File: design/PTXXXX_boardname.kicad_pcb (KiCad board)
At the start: 4 copper layers, 150 x 100 mm, 5 parts

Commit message: changed to 0.20/0.20mm track/gap design rules match F.Fab text ...though F.Fab text previously had gap less than design rules ...picked new sensible based on Qucs studio calc 89.3ohm Zdiff
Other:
- board text added: "INSTRUCTIONS: =========== MULTILAYER, SURFACE MOUNT & THROUGH HOLE 4 (2 SIGNAL & POUR, 2 SPLIT PLANE) MIN 0.20MM TRACK / 0.20MM GAP / 0.30MM DRILL 90Z DIFF PAIR, OUTER 0.20MM TRACK / 0.20MM GAP 0.40MM PLANE CLEARANCE, 0.12MM TO INNER FR4 OR EQUIVALENT, PCB RATED UL94V-0 35um OUTERS AND 17.5um INNERS ENIG GREEN WHITE 100.0MM X 150.0MM 1.6MM +/- 10% MAX OVER PLATING NOT REQUIRED NOT REQUIRED NOT RE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"
- board text removed: "INSTRUCTIONS: =========== MULTILAYER, SURFACE MOUNT & THROUGH HOLE 4 (2 SIGNAL & POUR, 2 SPLIT PLANE) MIN 0.2MM TRACK / 0.20MM GAP / 0.30MM DRILL 90Z DIFF PAIR, OUTER (0.25MM TRACK / 0.15MM GAP / 0.12MM TO INNER) FR4 OR EQUIVALENT, PCB RATED UL94V-0 35um OUTERS AND 17.5um INNERS ENIG GREEN WHITE 100.0MM X 150.0MM 1.6MM +/- 10% MAX OVER PLATING NOT REQUIRED NOT REQUIRED NOT REQUIRED SEEK APPROVAL 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"
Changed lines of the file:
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@@
       (layer "B.SilkS" (type "Bottom Silk Screen") (color "White"))
       (copper_finish "ENIG")
-      (dielectric_constraints no)
+      (dielectric_constraints yes)
     )
     (pad_to_mask_clearance 0.065)
@@
     (effects (font (size 2.5 2.5) (thickness 0.25) italic) (justify left))
   )
-  (gr_text "FABRICATION\n===========\nSUMMARY:\nLAYER COUNT:\nDESIGN RULES:\nIMPEDANCE CONTROL:\n\nMATERIAL:\nCOPPER WEIGHT:\nFINISH:\nRESIST COLOUR:\nSILKSCREEN COLOUR:\nDIMENSIONS:\nFINISHED THICKNESS:\nEDGE PLATING:\nEDGE CONNECTORS:\nEDGE CHAMFERING:\nTHIEVING/VENTING:\nROHS/LEAD FREE:\nDRILLING:\nPLUGGING:\nOTHER NOTES:" (at 225.2 114.9) (layer "F.Fab")
+  (gr_text "FABRICATION\n===========\nSUMMARY:\nLAYER COUNT:\nDESIGN RULES:\nIMPEDANCE CONTROL:\n\n\nMATERIAL:\nCOPPER WEIGHT:\nFINISH:\nRESIST COLOUR:\nSILKSCREEN COLOUR:\nDIMENSIONS:\nFINISHED THICKNESS:\nEDGE PLATING:\nEDGE CONNECTORS:\nEDGE CHAMFERING:\nTHIEVING/VENTING:\nROHS/LEAD FREE:\nDRILLING:\nPLUGGING:\nOTHER NOTES:" (at 225.2 114.9) (layer "F.Fab")
     (effects (font (size 1.2 1.2) (thickness 0.2)) (justify right))
   )
-  (gr_text "INSTRUCTIONS:\n===========\nMULTILAYER, SURFACE MOUNT & THROUGH HOLE\n4 (2 SIGNAL & POUR, 2 SPLIT PLANE)\nMIN 0.2MM TRACK / 0.20MM GAP / 0.30MM DRILL\n90Z DIFF PAIR, OUTER\n    (0.25MM TRACK / 0.15MM GAP / 0.12MM TO INNER)\nFR4 OR EQUIVALENT, PCB RATED UL94V-0\n35um OUTERS AND 17.5um INNERS\nENIG\nGREEN\nWHITE\n100.0MM X 150.0MM\n1.6MM +/- 10% MAX OVER PLATING\nNOT REQUIRED\nNOT REQUIRED\nNOT REQUIRED\nSEEK APPROVAL\nYES\nSEE DRILL FILE. HOLE SIZES ARE FINISHED.\nNOT REQUIRED\nNONE" (at 226.2 114.9) (layer "F.Fab")
+  (gr_text "INSTRUCTIONS:\n===========\nMULTILAYER, SURFACE MOUNT & THROUGH HOLE\n4 (2 SIGNAL & POUR, 2 SPLIT PLANE)\nMIN 0.20MM TRACK / 0.20MM GAP / 0.30MM DRILL\n90Z DIFF PAIR, OUTER\n    0.20MM TRACK / 0.20MM GAP\n    0.40MM PLANE CLEARANCE, 0.12MM TO INNER\nFR4 OR EQUIVALENT, PCB RATED UL94V-0\n35um OUTERS AND 17.5um INNERS\nENIG\nGREEN\nWHITE\n100.0MM X 150.0MM\n1.6MM +/- 10% MAX OVER PLATING\nNOT REQUIRED\nNOT REQUIRED\nNOT REQUIRED\nSEEK APPROVAL\nYES\nSEE DRILL FILE. HOLE SIZES ARE FINISHED.\nNOT REQUIRED\nNONE" (at 226.2 114.9) (layer "F.Fab")
     (effects (font (size 1.2 1.2) (thickness 0.2)) (justify left))
   )

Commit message: fixes for edge clearance issue in v6... ...moved 'Margin' line to Eco2 layer ...(Margin interferes with copper in v6) ...changed Margin layer text from "Board Edge Placement Margin" ...now text "Board Edge Copper Margin" changed schematic DRCs rules to reduce number... ...changed library symbol from warning to ignore (too many) updated library ref for latest
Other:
- board text added: "Layer Name: Margin Layer Description: Board Edge Copper Margin"
- board text removed: "Layer Name: Margin Layer Description: Board Edge Placement Margin"
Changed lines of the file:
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@@
       (xy 58.6 154.1)
     ) (layer "F.SilkS") (width 0.1) (fill solid))
+  (gr_line (start 188.5 158.5) (end 41.5 158.5) (layer "Eco2.User") (width 0.15))
+  (gr_line (start 41.5 61.5) (end 188.5 61.5) (layer "Eco2.User") (width 0.15))
+  (gr_line (start 188.5 61.5) (end 188.5 158.5) (layer "Eco2.User") (width 0.15))
+  (gr_line (start 41.5 158.5) (end 41.5 61.5) (layer "Eco2.User") (width 0.15))
   (gr_line (start 40 60) (end 40 160) (layer "Edge.Cuts") (width 0.05))
   (gr_line (start 190 160) (end 190 60) (layer "Edge.Cuts") (width 0.05))
   (gr_line (start 190 60) (end 40 60) (layer "Edge.Cuts") (width 0.05))
   (gr_line (start 40 160) (end 190 160) (layer "Edge.Cuts") (width 0.05))
-  (gr_line (start 188.5 158.5) (end 41.5 158.5) (layer "Margin") (width 0.15))
-  (gr_line (start 41.5 61.5) (end 188.5 61.5) (layer "Margin") (width 0.15))
-  (gr_line (start 188.5 61.5) (end 188.5 158.5) (layer "Margin") (width 0.15))
-  (gr_line (start 41.5 158.5) (end 41.5 61.5) (layer "Margin") (width 0.15))
   (gr_poly
     (pts
@@
     (effects (font (size 2.5 2.5) (thickness 0.25) italic) (justify left))
   )
-  (gr_text "Layer Name:          Margin\nLayer Description:    Board Edge Placement Margin" (at 67.2 27.4) (layer "Margin")
+  (gr_text "Layer Name:          Margin\nLayer Description:    Board Edge Copper Margin" (at 67.2 27.4) (layer "Margin")
     (effects (font (size 2.5 2.5) (thickness 0.25) italic) (justify left))
   )

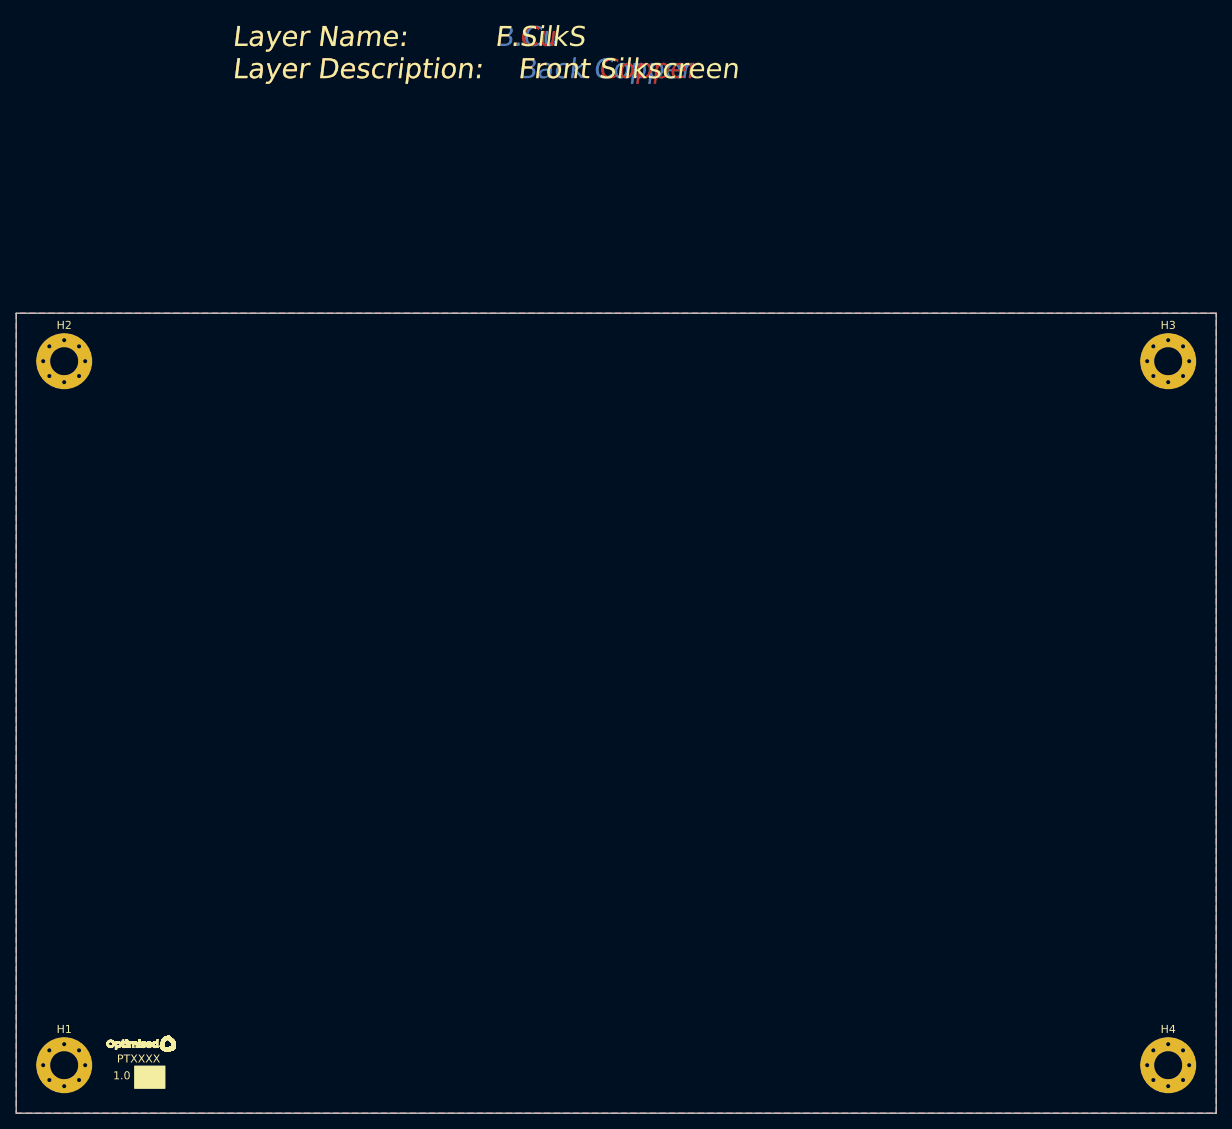
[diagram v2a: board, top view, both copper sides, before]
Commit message: added Fiducials FID1-6 using new library part... ...3off top, 3off bottom, 1mm/3mm mask default but 2mm available ...annotated, netlisted, placed in PCB updated library ref for latest
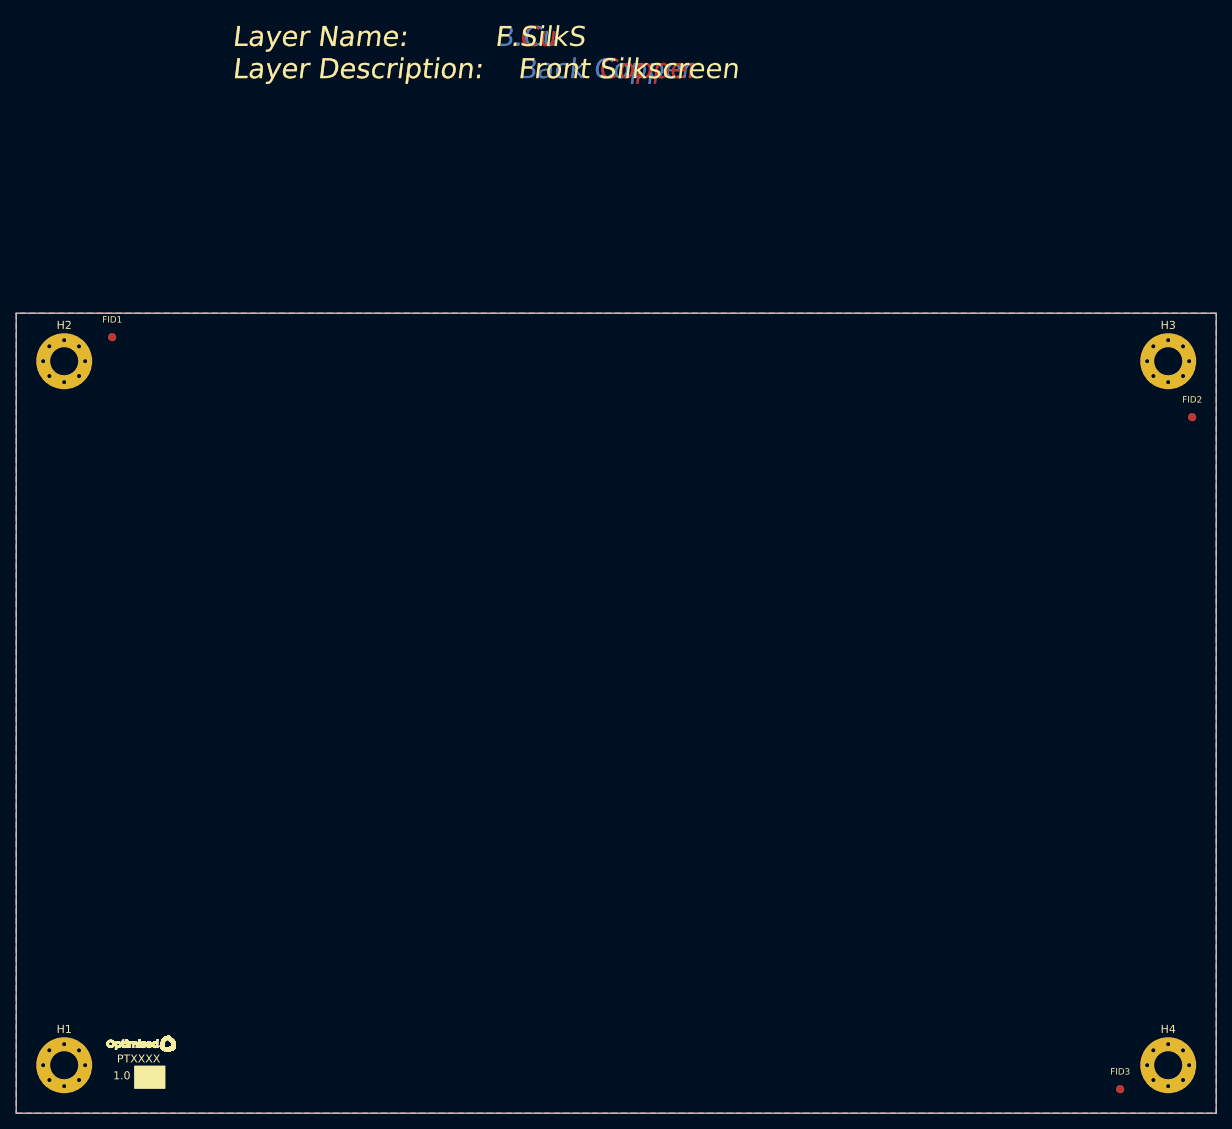
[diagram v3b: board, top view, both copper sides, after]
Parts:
- added FID1: Fiducial, _kb_miscellaneous:Fiducial_1mm_Mask3mm, F.Cu at (52.0, 63.0)
- added FID2: Fiducial, _kb_miscellaneous:Fiducial_1mm_Mask3mm, F.Cu at (187.0, 73.0)
- added FID3: Fiducial, _kb_miscellaneous:Fiducial_1mm_Mask3mm, F.Cu at (178.0, 157.0)
- added FID4: Fiducial, _kb_miscellaneous:Fiducial_1mm_Mask3mm, B.Cu at (178.0, 157.0)
- added FID5: Fiducial, _kb_miscellaneous:Fiducial_1mm_Mask3mm, B.Cu at (187.0, 73.0)
- added FID6: Fiducial, _kb_miscellaneous:Fiducial_1mm_Mask3mm, B.Cu at (52.0, 63.0)
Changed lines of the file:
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@@
       ) (layer "F.SilkS") (width 0.01) (fill solid))
+  )
+  (footprint "_kb_miscellaneous:Fiducial_1mm_Mask3mm" (layer "F.Cu")
+    (at 187 73)
+    (descr "Circular Fiducial, 1mm bare copper, 3mm soldermask opening (recommended)")
+    (tags "fiducial")
+    (property "Description" "Fiducial Assembly Marker")
+    (property "FitPart" "DNF")
+    (property "MPN1" "N/A")
+    (property "MPN2" " ")
+    (property "Manufacturer1" "N/A")
+    (property "Manufacturer2" " ")
+    (property "SKU1" " ")
+    (property "SKU2" " ")
+    (property "Sheetfile" "PTXXXX_boardname.kicad_sch")
+    (property "Sheetname" "")
+    (property "Vendor1" " ")
+    (property "Vendor2" " ")
+    (attr smd)
+    (fp_text reference "FID2" (at 0 -2.2) (layer "F.SilkS")
+      (effects (font (size 0.8 0.8) (thickness 0.12)))
+    )
+    (fp_text value "Fiducial" (at 0 2.286) (layer "F.Fab") hide
+      (effects (font (size 1 1) (thickness 0.15)))
+    )
+    (fp_text user "${REFERENCE}" (at 0 0) (layer "F.Fab")
+      (effects (font (size 0.6 0.6) (thickness 0.1)))
+    )
+    (fp_circle (center 0 0) (end 1.6 0) (layer "F.CrtYd") (width 0.05) (fill none))
+    (fp_circle (center 0 0) (end 1.5 0) (layer "F.Fab") (width 0.1) (fill none))
+    (pad "" smd circle (at 0 0) (size 1 1) (property pad_prop_fiducial_glob) (layers "F.Cu" "F.Mask")
+      (solder_mask_margin 1) (clearance 1))
+  )
+  (footprint "_kb_miscellaneous:Fiducial_1mm_Mask3mm" (layer "F.Cu")
+    (at 178 157)
+    (descr "Circular Fiducial, 1mm bare copper, 3mm soldermask opening (recommended)")
+    (tags "fiducial")
+    (property "Description" "Fiducial Assembly Marker")
+    (property "FitPart" "DNF")
+    (property "MPN1" "N/A")
+    (property "MPN2" " ")
+    (property "Manufacturer1" "N/A")
+    (property "Manufacturer2" " ")
+    (property "SKU1" " ")
+    (property "SKU2" " ")
+    (property "Sheetfile" "PTXXXX_boardname.kicad_sch")
+    (property "Sheetname" "")
+    (property "Vendor1" " ")
+    (property "Vendor2" " ")
+    (attr smd)
+    (fp_text reference "FID3" (at 0 -2.2) (layer "F.SilkS")
+      (effects (font (size 0.8 0.8) (thickness 0.12)))
+    )
+    (fp_text value "Fiducial" (at 0 2.286) (layer "F.Fab") hide
+      (effects (font (size 1 1) (thickness 0.15)))
+    )
+    (fp_text user "${REFERENCE}" (at 0 0) (layer "F.Fab")
+      (effects (font (size 0.6 0.6) (thickness 0.1)))
+    )
+    (fp_circle (center 0 0) (end 1.6 0) (layer "F.CrtYd") (width 0.05) (fill none))
+    (fp_circle (center 0 0) (end 1.5 0) (layer "F.Fab") (width 0.1) (fill none))
+    (pad "" smd circle (at 0 0) (size 1 1) (property pad_prop_fiducial_glob) (layers "F.Cu" "F.Mask")
+      (solder_mask_margin 1) (clearance 1))
+  )
+  (footprint "_kb_miscellaneous:Fiducial_1mm_Mask3mm" (layer "F.Cu")
+    (at 52 63)
+    (descr "Circular Fiducial, 1mm bare copper, 3mm soldermask opening (recommended)")
+    (tags "fiducial")
+    (property "Description" "Fiducial Assembly Marker")
+    (property "FitPart" "DNF")
+    (property "MPN1" "N/A")
+    (property "MPN2" " ")
+    (property "Manufacturer1" "N/A")
+    (property "Manufacturer2" " ")
+    (property "SKU1" " ")
+    (property "SKU2" " ")
+    (property "Sheetfile" "PTXXXX_boardname.kicad_sch")
+    (property "Sheetname" "")
+    (property "Vendor1" " ")
+    (property "Vendor2" " ")
+    (attr smd)
+    (fp_text reference "FID1" (at 0 -2.2) (layer "F.SilkS")
+      (effects (font (size 0.8 0.8) (thickness 0.12)))
+    )
+    (fp_text value "Fiducial" (at 0 2.286) (layer "F.Fab") hide
+      (effects (font (size 1 1) (thickness 0.15)))
+    )
+    (fp_text user "${REFERENCE}" (at 0 0) (layer "F.Fab")
+      (effects (font (size 0.6 0.6) (thickness 0.1)))
+    )
+    (fp_circle (center 0 0) (end 1.6 0) (layer "F.CrtYd") (width 0.05) (fill none))
+    (fp_circle (center 0 0) (end 1.5 0) (layer "F.Fab") (width 0.1) (fill none))
+    (pad "" smd circle (at 0 0) (size 1 1) (property pad_prop_fiducial_glob) (layers "F.Cu" "F.Mask")
+      (solder_mask_margin 1) (clearance 1))
+  )
+  (footprint "_kb_miscellaneous:Fiducial_1mm_Mask3mm" (layer "B.Cu")
+    (at 187 73 180)
+    (descr "Circular Fiducial, 1mm bare copper, 3mm soldermask opening (recommended)")
+    (tags "fiducial")
+    (property "Description" "Fiducial Assembly Marker")
+    (property "FitPart" "DNF")
+    (property "MPN1" "N/A")
+    (property "MPN2" " ")
+    (property "Manufacturer1" "N/A")
+    (property "Manufacturer2" " ")
+    (property "SKU1" " ")
+    (property "SKU2" " ")
+    (property "Sheetfile" "PTXXXX_boardname.kicad_sch")
+    (property "Sheetname" "")
+    (property "Vendor1" " ")
+    (property "Vendor2" " ")
+    (attr smd)
+    (fp_text reference "FID5" (at 0 2.2) (layer "B.SilkS")
+      (effects (font (size 0.8 0.8) (thickness 0.12)) (justify mirror))
+    )
+    (fp_text value "Fiducial" (at 0 -2.286) (layer "B.Fab") hide
+      (effects (font (size 1 1) (thickness 0.15)) (justify mirror))
+    )
+    (fp_text user "${REFERENCE}" (at 0 0) (layer "B.Fab")
+      (effects (font (size 0.6 0.6) (thickness 0.1)) (justify mirror))
+    )
+    (fp_circle (center 0 0) (end 1.6 0) (layer "B.CrtYd") (width 0.05) (fill none))
+    (fp_circle (center 0 0) (end 1.5 0) (layer "B.Fab") (width 0.1) (fill none))
+    (pad "" smd circle (at 0 0 180) (size 1 1) (property pad_prop_fiducial_glob) (layers "B.Cu" "B.Mask")
+      (solder_mask_margin 1) (clearance 1))
+  )
+  (footprint "_kb_miscellaneous:Fiducial_1mm_Mask3mm" (layer "B.Cu")
+    (at 52 63 180)
+    (descr "Circular Fiducial, 1mm bare copper, 3mm soldermask opening (recommended)")
+    (tags "fiducial")
+    (property "Description" "Fiducial Assembly Marker")
+    (property "FitPart" "DNF")
+    (property "MPN1" "N/A")
+    (property "MPN2" " ")
+    (property "Manufacturer1" "N/A")
+    (property "Manufacturer2" " ")
+    (property "SKU1" " ")
+    (property "SKU2" " ")
+    (property "Sheetfile" "PTXXXX_boardname.kicad_sch")
+    (property "Sheetname" "")
+    (property "Vendor1" " ")
+    (property "Vendor2" " ")
+    (attr smd)
+    (fp_text reference "FID6" (at 0 2.2) (layer "B.SilkS")
+      (effects (font (size 0.8 0.8) (thickness 0.12)) (justify mirror))
+    )
+    (fp_text value "Fiducial" (at 0 -2.286) (layer "B.Fab") hide
+      (effects (font (size 1 1) (thickness 0.15)) (justify mirror))
+    )
+    (fp_text user "${REFERENCE}" (at 0 0) (layer "B.Fab")
+      (effects (font (size 0.6 0.6) (thickness 0.1)) (justify mirror))
+    )
+    (fp_circle (center 0 0) (end 1.6 0) (layer "B.CrtYd") (width 0.05) (fill none))
+    (fp_circle (center 0 0) (end 1.5 0) (layer "B.Fab") (width 0.1) (fill none))
+    (pad "" smd circle (at 0 0 180) (size 1 1) (property pad_prop_fiducial_glob) (layers "B.Cu" "B.Mask")
+      (solder_mask_margin 1) (clearance 1))
+  )
+  (footprint "_kb_miscellaneous:Fiducial_1mm_Mask3mm" (layer "B.Cu")
+    (at 178 157 180)
+    (descr "Circular Fiducial, 1mm bare copper, 3mm soldermask opening (recommended)")
+    (tags "fiducial")
+    (property "Description" "Fiducial Assembly Marker")
+    (property "FitPart" "DNF")
+    (property "MPN1" "N/A")
+    (property "MPN2" " ")
+    (property "Manufacturer1" "N/A")
+    (property "Manufacturer2" " ")
+    (property "SKU1" " ")
+    (property "SKU2" " ")
+    (property "Sheetfile" "PTXXXX_boardname.kicad_sch")
+    (property "Sheetname" "")
+    (property "Vendor1" " ")
+    (property "Vendor2" " ")
+    (attr smd)
+    (fp_text reference "FID4" (at 0 2.2) (layer "B.SilkS")
+      (effects (font (size 0.8 0.8) (thickness 0.12)) (justify mirror))
+    )
+    (fp_text value "Fiducial" (at 0 -2.286) (layer "B.Fab") hide
+      (effects (font (size 1 1) (thickness 0.15)) (justify mirror))
+    )
+    (fp_text user "${REFERENCE}" (at 0 0) (layer "B.Fab")
+      (effects (font (size 0.6 0.6) (thickness 0.1)) (justify mirror))
+    )
+    (fp_circle (center 0 0) (end 1.6 0) (layer "B.CrtYd") (width 0.05) (fill none))
+    (fp_circle (center 0 0) (end 1.5 0) (layer "B.Fab") (width 0.1) (fill none))
+    (pad "" smd circle (at 0 0 180) (size 1 1) (property pad_prop_fiducial_glob) (layers "B.Cu" "B.Mask")
+      (solder_mask_margin 1) (clearance 1))
   )
   (gr_poly
@@
   (zone (net 1) (net_name "GND") (layer "F.Cu") (hatch edge 0.508)
     (connect_pads (clearance 0.4))
-    (min_thickness 0.25)
+    (min_thickness 0.25) (filled_areas_thickness no)
     (fill yes (thermal_gap 0.251) (thermal_bridge_width 0.251))
     (polygon
@@
   (zone (net 1) (net_name "GND") (layer "In1.Cu") (hatch edge 0.508)
     (connect_pads (clearance 0.4))
-    (min_thickness 0.25)
+    (min_thickness 0.25) (filled_areas_thickness no)
     (fill yes (thermal_gap 0.251) (thermal_bridge_width 0.251))
     (polygon
@@
   (zone (net 1) (net_name "GND") (layer "In2.Cu") (hatch edge 0.508)
     (connect_pads (clearance 0.4))
-    (min_thickness 0.25)
+    (min_thickness 0.25) (filled_areas_thickness no)
     (fill yes (thermal_gap 0.251) (thermal_bridge_width 0.251))
     (polygon
@@
   (zone (net 1) (net_name "GND") (layer "B.Cu") (hatch edge 0.508)
     (connect_pads (clearance 0.4))
-    (min_thickness 0.25)
+    (min_thickness 0.25) (filled_areas_thickness no)
     (fill yes (thermal_gap 0.251) (thermal_bridge_width 0.251))
     (polygon
